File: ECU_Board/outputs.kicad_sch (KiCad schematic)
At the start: 20 parts, among them J4 Conn_01x06, Q1 SSM3K318R, Q2 SSM3K318R, Q3 SSM3K318R, U8 BM2LC105, U9 BM2LC105

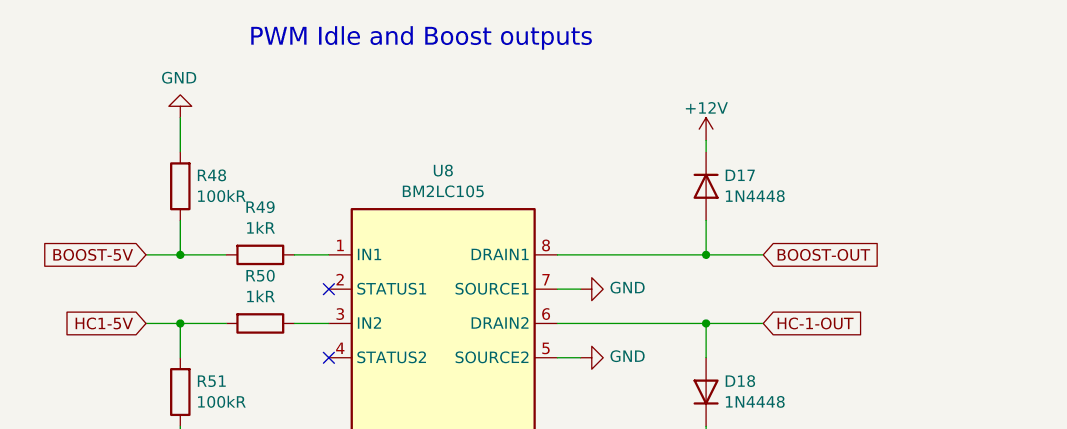
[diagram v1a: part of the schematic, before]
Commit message: Changed Boost output to ACIS
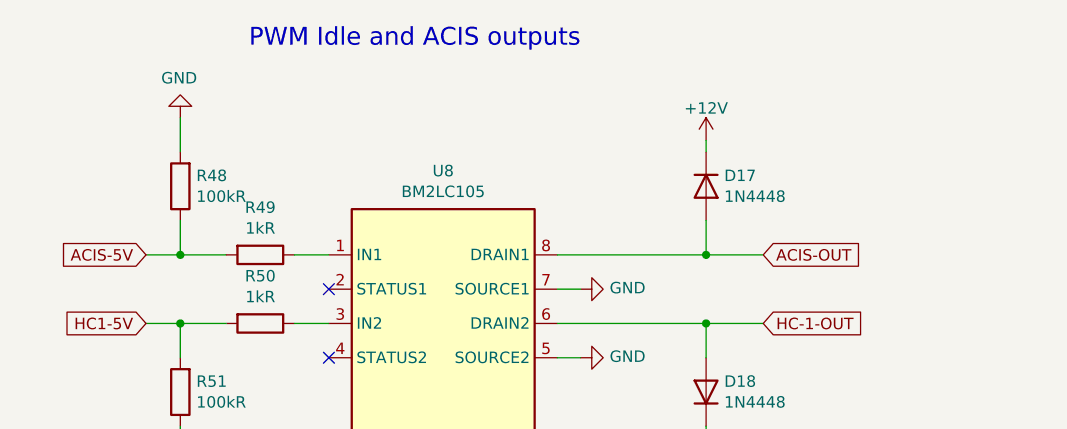
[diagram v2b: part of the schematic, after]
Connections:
- net BOOST-5V renamed ACIS-5V
- net BOOST-OUT renamed ACIS-OUT
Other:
- note added: "PWM Idle and ACIS outputs"
- note removed: "PWM Idle and Boost outputs"
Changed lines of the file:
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@@
     (effects (font (size 1.9812 1.9812)) (justify left bottom))
   )
-  (text "PWM Idle and Boost outputs" (at 46.99 20.32 0)
+  (text "PWM Idle and ACIS outputs" (at 46.99 20.32 0)
     (effects (font (size 1.9812 1.9812)) (justify left bottom))
   )
@@
     )
   )
-  (global_label "BOOST-OUT" (shape input) (at 104.14 43.18 0) (fields_autoplaced)
+  (global_label "ACIS-OUT" (shape input) (at 104.14 43.18 0) (fields_autoplaced)
     (effects (font (size 1.27 1.27)) (justify left))
-    (property "Intersheet References" "${INTERSHEET_REFS}" (id 0) (at 117.8621 43.1006 0)
+    (property "Intersheet References" "${INTERSHEET_REFS}" (id 0) (at 115.9269 43.1006 0)
       (effects (font (size 1.27 1.27)) (justify left) hide)
     )
@@
     )
   )
-  (global_label "BOOST-5V" (shape input) (at 35.56 43.18 180) (fields_autoplaced)
+  (global_label "ACIS-5V" (shape input) (at 35.56 43.18 180) (fields_autoplaced)
     (effects (font (size 1.27 1.27)) (justify right))
-    (property "Intersheet References" "${INTERSHEET_REFS}" (id 0) (at 23.1683 43.1006 0)
+    (property "Intersheet References" "${INTERSHEET_REFS}" (id 0) (at 25.1036 43.1006 0)
       (effects (font (size 1.27 1.27)) (justify right) hide)
     )

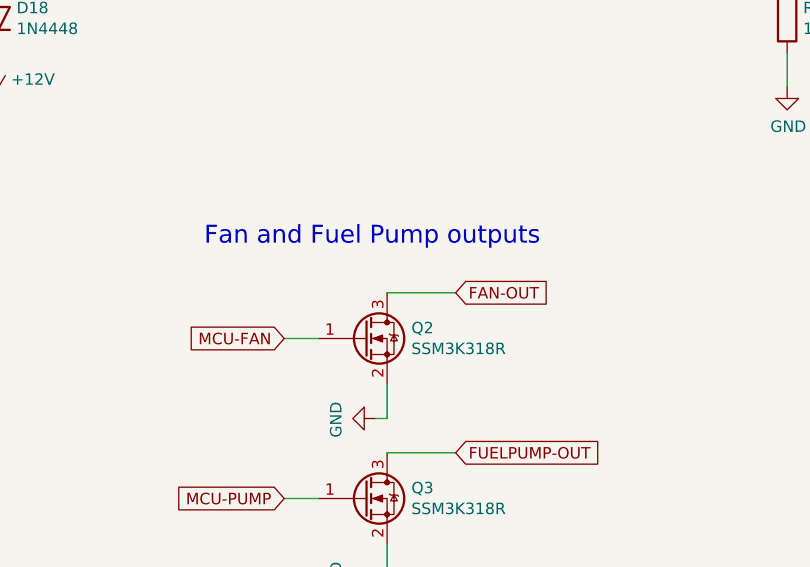
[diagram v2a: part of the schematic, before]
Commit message: Finished adapter board, slight changes to ECU
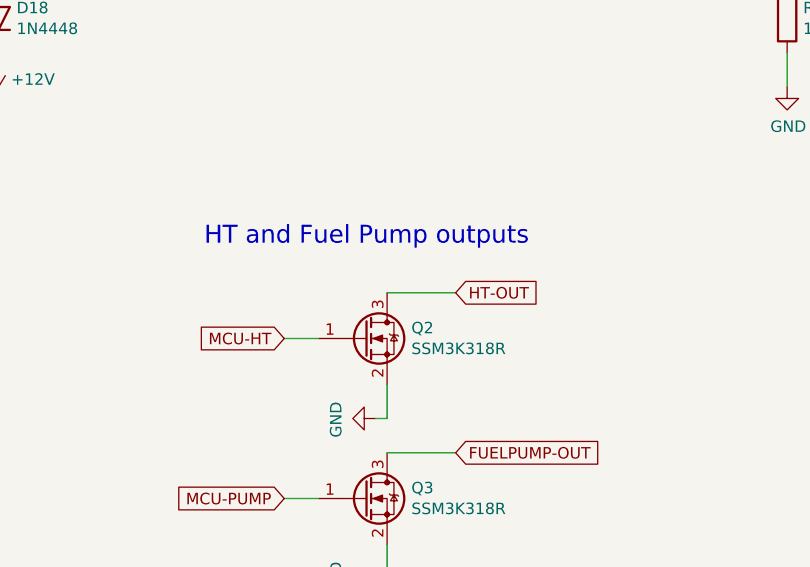
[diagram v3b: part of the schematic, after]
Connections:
- net FAN-OUT renamed HT-OUT
- net MCU-FAN renamed MCU-HT
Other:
- note added: "HT and Fuel Pump outputs"
- note removed: "Fan and Fuel Pump outputs"
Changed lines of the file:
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@@
     (stroke (width 0) (type default) (color 0 0 0 0))
   )
-  (text "Fan and Fuel Pump outputs" (at 120.65 83.82 0)
+  (text "HT and Fuel Pump outputs" (at 120.65 83.82 0)
     (effects (font (size 1.9812 1.9812)) (justify left bottom))
   )
@@
     )
   )
-  (global_label "FAN-OUT" (shape input) (at 148.59 88.9 0) (fields_autoplaced)
+  (global_label "HT-OUT" (shape input) (at 148.59 88.9 0) (fields_autoplaced)
     (effects (font (size 1.27 1.27)) (justify left))
-    (property "Intersheet References" "${INTERSHEET_REFS}" (id 0) (at 0 0 0)
-      (effects (font (size 1.27 1.27)) hide)
+    (property "Intersheet References" "${INTERSHEET_REFS}" (id 0) (at 158.5021 88.8206 0)
+      (effects (font (size 1.27 1.27)) (justify left) hide)
     )
   )
@@
     )
   )
-  (global_label "MCU-FAN" (shape input) (at 129.54 93.98 180) (fields_autoplaced)
+  (global_label "MCU-HT" (shape input) (at 129.54 93.98 180) (fields_autoplaced)
     (effects (font (size 1.27 1.27)) (justify right))
-    (property "Intersheet References" "${INTERSHEET_REFS}" (id 0) (at 117.995 93.9006 0)
+    (property "Intersheet References" "${INTERSHEET_REFS}" (id 0) (at 119.2045 93.9006 0)
       (effects (font (size 1.27 1.27)) (justify right) hide)
     )
